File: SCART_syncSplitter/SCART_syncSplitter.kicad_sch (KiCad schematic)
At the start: 28 parts, among them J1 SCART-F, J2 VGA Out, J3 POWER IN, J4 HSync Selector, J5 Audio Out, U1 LMH1981, U2 L7805

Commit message: Assigned footprints
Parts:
- added C9: 10uF, Capacitor_THT:CP_Radial_D5.0mm_P2.50mm, symbol Device:C_Polarized_Small
- added JP2: VGA_PWR, Jumper:SolderJumper-2_P1.3mm_Open_RoundedPad1.0x1.5mm, symbol Jumper:SolderJumper_2_Open
- C8: value 10uF -> 4.7uF; footprint (none) -> Capacitor_THT:CP_Radial_D5.0mm_P2.50mm
- J2: footprint (none) -> Connector_Dsub:DSUB-15-HD_Female_Horizontal_P2.29x1.98mm_EdgePinOffset3.03mm_Housed_MountingHolesOffset4.94mm
- J3: footprint (none) -> Connector_BarrelJack:BarrelJack_Horizontal
- J4: footprint (none) -> Connector_PinHeader_2.54mm:PinHeader_2x02_P2.54mm_Vertical
- JP1: footprint (none) -> Connector_PinHeader_2.54mm:PinHeader_1x02_P2.54mm_Vertical
- TP1, TP2, TP3: footprint (none) -> TestPoint:TestPoint_Pad_1.0x1.0mm
- U2: footprint (none) -> Package_TO_SOT_SMD:TO-263-3_TabPin2
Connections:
- net GND: now also C9.2
- net VCC: now also C8.1, JP2.1 (A); no longer J2.9
- net at C7.1, J3.1 (In), U2.1 (IN): now also C9.1; no longer C8.1
- new net: J2.9, JP2.2 (B)
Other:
- moved on the sheet: C8
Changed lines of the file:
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@@
   (junction (at 97.79 39.37) (diameter 0) (color 0 0 0 0)
   )
+  (junction (at 135.89 24.13) (diameter 0) (color 0 0 0 0)
+  )
   (junction (at 19.05 137.16) (diameter 0) (color 0 0 0 0)
   )
@@
   )
   (junction (at 177.8 129.54) (diameter 0) (color 0 0 0 0)
+  )
+  (junction (at 128.27 39.37) (diameter 0) (color 0 0 0 0)
   )
   (junction (at 88.9 160.02) (diameter 0) (color 0 0 0 0)
@@
     (stroke (width 0) (type default))
   )
+  (wire (pts (xy 194.31 134.62) (xy 198.12 134.62))
+    (stroke (width 0) (type default))
+  )
   (wire (pts (xy 87.63 76.2) (xy 107.95 76.2))
     (stroke (width 0) (type default))
@@
     (stroke (width 0) (type default))
   )
+  (wire (pts (xy 128.27 39.37) (xy 135.89 39.37))
+    (stroke (width 0) (type default))
+  )
   (wire (pts (xy 198.12 129.54) (xy 177.8 129.54))
     (stroke (width 0) (type default))
@@
     (stroke (width 0) (type default))
   )
-  (wire (pts (xy 180.34 134.62) (xy 198.12 134.62))
+  (wire (pts (xy 135.89 39.37) (xy 135.89 34.29))
     (stroke (width 0) (type default))
   )
@@
     (stroke (width 0) (type default))
   )
+  (wire (pts (xy 180.34 134.62) (xy 186.69 134.62))
+    (stroke (width 0) (type default))
+  )
   (wire (pts (xy 120.65 130.81) (xy 120.65 134.62))
     (stroke (width 0) (type default))
@@
     (stroke (width 0) (type default))
   )
+  (wire (pts (xy 128.27 24.13) (xy 135.89 24.13))
+    (stroke (width 0) (type default))
+  )
   (wire (pts (xy 35.56 21.59) (xy 35.56 22.86))
     (stroke (width 0) (type default))
@@
     (stroke (width 0) (type default))
   )
+  (wire (pts (xy 135.89 24.13) (xy 135.89 29.21))
+    (stroke (width 0) (type default))
+  )
   (wire (pts (xy 184.15 127) (xy 198.12 127))
     (stroke (width 0) (type default))
@@
     (stroke (width 0) (type default))
   )
-  (wire (pts (xy 128.27 20.32) (xy 128.27 24.13))
+  (wire (pts (xy 135.89 20.32) (xy 135.89 24.13))
     (stroke (width 0) (type default))
   )
@@
       (effects (font (size 1.27 1.27)))
     )
-    (property "Footprint" "" (at 181.61 121.92 0)
+    (property "Footprint" "Connector_Dsub:DSUB-15-HD_Female_Horizontal_P2.29x1.98mm_EdgePinOffset3.03mm_Housed_MountingHolesOffset4.94mm" (at 181.61 121.92 0)
       (effects (font (size 1.27 1.27)) hide)
     )
@@
       (effects (font (size 1.27 1.27)) (justify left))
     )
-    (property "Footprint" "" (at 77.47 54.61 0)
+    (property "Footprint" "TestPoint:TestPoint_Pad_1.0x1.0mm" (at 77.47 54.61 0)
       (effects (font (size 1.27 1.27)) hide)
     )
@@
       (effects (font (size 1.27 1.27)))
     )
-    (property "Footprint" "" (at 240.03 135.89 0)
+    (property "Footprint" "Connector_PinHeader_2.54mm:PinHeader_2x02_P2.54mm_Vertical" (at 240.03 135.89 0)
       (effects (font (size 1.27 1.27)) hide)
     )
@@
     )
   )
-  (symbol (lib_id "power:VCC") (at 128.27 20.32 0) (unit 1)
+  (symbol (lib_id "power:VCC") (at 135.89 20.32 0) (unit 1)
     (in_bom yes) (on_board yes) (dnp no) (fields_autoplaced)
-    (property "Reference" "#PWR012" (at 128.27 24.13 0)
-      (effects (font (size 1.27 1.27)) hide)
-    )
-    (property "Value" "VCC" (at 128.27 15.24 0)
-      (effects (font (size 1.27 1.27)))
-    )
-    (property "Footprint" "" (at 128.27 20.32 0)
-      (effects (font (size 1.27 1.27)) hide)
-    )
-    (property "Datasheet" "" (at 128.27 20.32 0)
+    (property "Reference" "#PWR012" (at 135.89 24.13 0)
+      (effects (font (size 1.27 1.27)) hide)
+    )
+    (property "Value" "VCC" (at 135.89 15.24 0)
+      (effects (font (size 1.27 1.27)))
+    )
+    (property "Footprint" "" (at 135.89 20.32 0)
+      (effects (font (size 1.27 1.27)) hide)
+    )
+    (property "Datasheet" "" (at 135.89 20.32 0)
       (effects (font (size 1.27 1.27)) hide)
     )
@@
       (effects (font (size 1.27 1.27)) (justify left))
     )
-    (property "Footprint" "" (at 88.9 33.02 0)
+    (property "Footprint" "Connector_BarrelJack:BarrelJack_Horizontal" (at 88.9 33.02 0)
       (effects (font (size 1.27 1.27)) hide)
     )
@@
       (effects (font (size 1.27 1.27)))
     )
-    (property "Footprint" "" (at 114.935 27.94 0)
+    (property "Footprint" "Package_TO_SOT_SMD:TO-263-3_TabPin2" (at 114.935 27.94 0)
       (effects (font (size 1.27 1.27) italic) (justify left) hide)
     )
@@
     )
   )
+  (symbol (lib_id "Device:C_Polarized_Small") (at 97.79 31.75 0) (unit 1)
+    (in_bom yes) (on_board yes) (dnp no)
+    (property "Reference" "C9" (at 95.25 33.02 90)
+      (effects (font (size 1.27 1.27)) (justify left))
+    )
+    (property "Value" "10uF" (at 100.33 34.29 90)
+      (effects (font (size 1.27 1.27)) (justify left))
+    )
+    (property "Footprint" "Capacitor_THT:CP_Radial_D5.0mm_P2.50mm" (at 97.79 31.75 0)
+      (effects (font (size 1.27 1.27)) hide)
+    )
+    (property "Datasheet" "~" (at 97.79 31.75 0)
+      (effects (font (size 1.27 1.27)) hide)
+    )
+    (pin "1")
+    (pin "2")
+    (instances
+      (project "SCART_syncSplitter"
+        (path "/99f02354-cbc7-4051-afde-370f4d1f5517"
+          (reference "C9") (unit 1)
+        )
+      )
+    )
+  )
   (symbol (lib_id "power:GND") (at 120.65 134.62 0) (unit 1)
     (in_bom yes) (on_board yes) (dnp no) (fields_autoplaced)
@@
       (effects (font (size 1.27 1.27)) (justify left))
     )
-    (property "Footprint" "" (at 113.03 66.04 0)
+    (property "Footprint" "TestPoint:TestPoint_Pad_1.0x1.0mm" (at 113.03 66.04 0)
       (effects (font (size 1.27 1.27)) hide)
     )
@@
         (path "/99f02354-cbc7-4051-afde-370f4d1f5517"
           (reference "TP3") (unit 1)
+        )
+      )
+    )
+  )
+  (symbol (lib_id "Jumper:SolderJumper_2_Open") (at 190.5 134.62 0) (unit 1)
+    (in_bom yes) (on_board yes) (dnp no)
+    (property "Reference" "JP2" (at 186.69 133.35 0)
+      (effects (font (size 1.27 1.27)))
+    )
+    (property "Value" "VGA_PWR" (at 195.58 133.35 0)
+      (effects (font (size 1.27 1.27)))
+    )
+    (property "Footprint" "Jumper:SolderJumper-2_P1.3mm_Open_RoundedPad1.0x1.5mm" (at 190.5 134.62 0)
+      (effects (font (size 1.27 1.27)) hide)
+    )
+    (property "Datasheet" "~" (at 190.5 134.62 0)
+      (effects (font (size 1.27 1.27)) hide)
+    )
+    (pin "1")
+    (pin "2")
+    (instances
+      (project "SCART_syncSplitter"
+        (path "/99f02354-cbc7-4051-afde-370f4d1f5517"
+          (reference "JP2") (unit 1)
         )
       )
@@
       (effects (font (size 1.27 1.27)) (justify left))
     )
-    (property "Footprint" "" (at 80.01 54.61 0)
+    (property "Footprint" "TestPoint:TestPoint_Pad_1.0x1.0mm" (at 80.01 54.61 0)
       (effects (font (size 1.27 1.27)) hide)
     )
@@
     )
   )
-  (symbol (lib_id "Device:C_Polarized_Small") (at 97.79 31.75 0) (unit 1)
-    (in_bom yes) (on_board yes) (dnp no)
-    (property "Reference" "C8" (at 95.25 33.02 90)
-      (effects (font (size 1.27 1.27)) (justify left))
-    )
-    (property "Value" "10uF" (at 100.33 34.29 90)
-      (effects (font (size 1.27 1.27)) (justify left))
-    )
-    (property "Footprint" "" (at 97.79 31.75 0)
-      (effects (font (size 1.27 1.27)) hide)
-    )
-    (property "Datasheet" "~" (at 97.79 31.75 0)
+  (symbol (lib_id "Device:C_Polarized_Small") (at 135.89 31.75 0) (unit 1)
+    (in_bom yes) (on_board yes) (dnp no)
+    (property "Reference" "C8" (at 133.35 33.02 90)
+      (effects (font (size 1.27 1.27)) (justify left))
+    )
+    (property "Value" "4.7uF" (at 138.43 34.29 90)
+      (effects (font (size 1.27 1.27)) (justify left))
+    )
+    (property "Footprint" "Capacitor_THT:CP_Radial_D5.0mm_P2.50mm" (at 135.89 31.75 0)
+      (effects (font (size 1.27 1.27)) hide)
+    )
+    (property "Datasheet" "~" (at 135.89 31.75 0)
       (effects (font (size 1.27 1.27)) hide)
     )
@@
       (effects (font (size 1.27 1.27)))
     )
-    (property "Footprint" "" (at 231.14 132.08 0)
-      (effects (font (size 1.27 1.27)) hide)
-    )
+    (property "Footprint" "Connector_PinHeader_2.54mm:PinHeader_1x02_P2.54mm_Vertical" (at 231.14 132.08 0)
+      (effects (font (size 1.27 1.27)) hide)
+    )

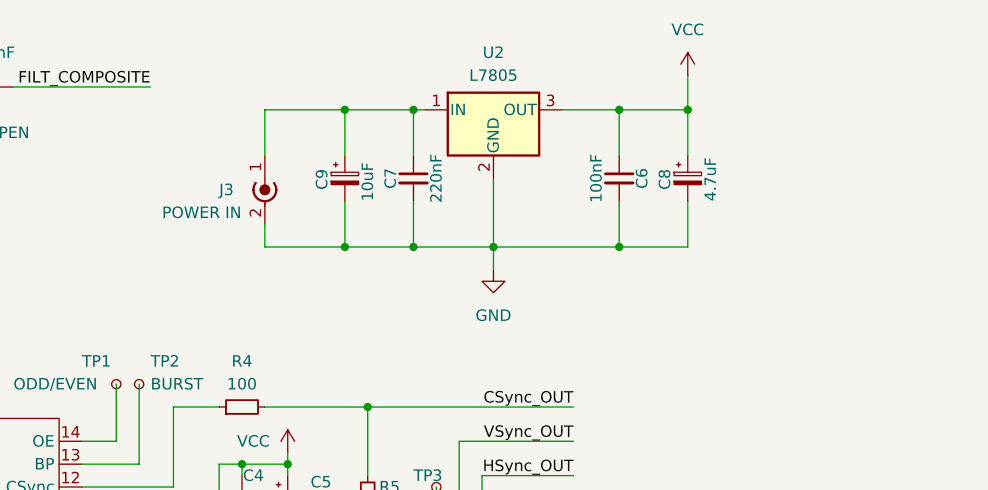
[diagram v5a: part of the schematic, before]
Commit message: Start preparing the PCB
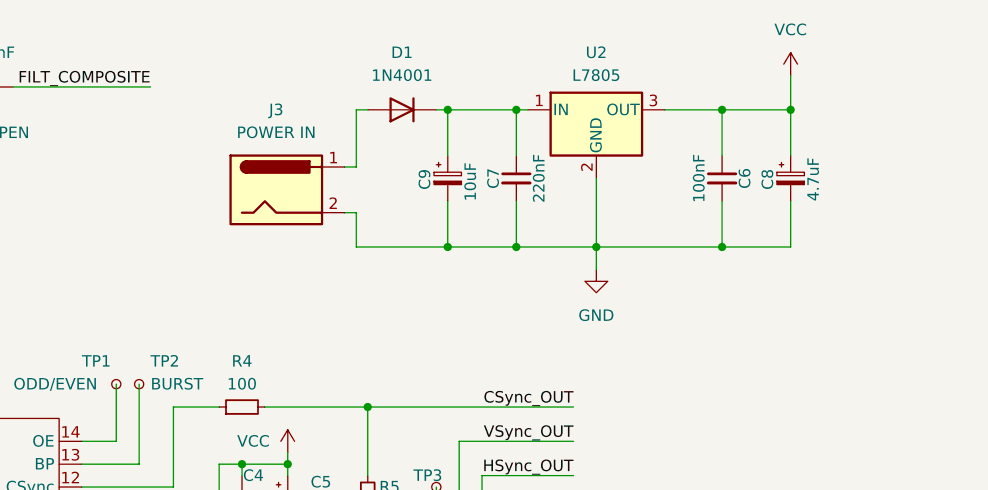
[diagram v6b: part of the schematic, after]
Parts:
- removed J3: POWER IN, Connector_BarrelJack:BarrelJack_Horizontal, symbol Connector:Conn_Coaxial_Power
- added D1: 1N4001, Diode_THT:D_DO-41_SOD81_P10.16mm_Horizontal, symbol Diode:1N4001
- added J3: POWER IN, Connector_BarrelJack:BarrelJack_Horizontal, symbol Connector:Barrel_Jack
- C5: footprint (none) -> Capacitor_THT:CP_Radial_D5.0mm_P2.50mm
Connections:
- net GND: now also J3.2
- net at C7.1, C9.1, U2.1 (IN): now also D1.1 (K)
- new net: D1.2 (A), J3.1
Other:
- moved on the sheet: C6, C7, C8, C9, U2

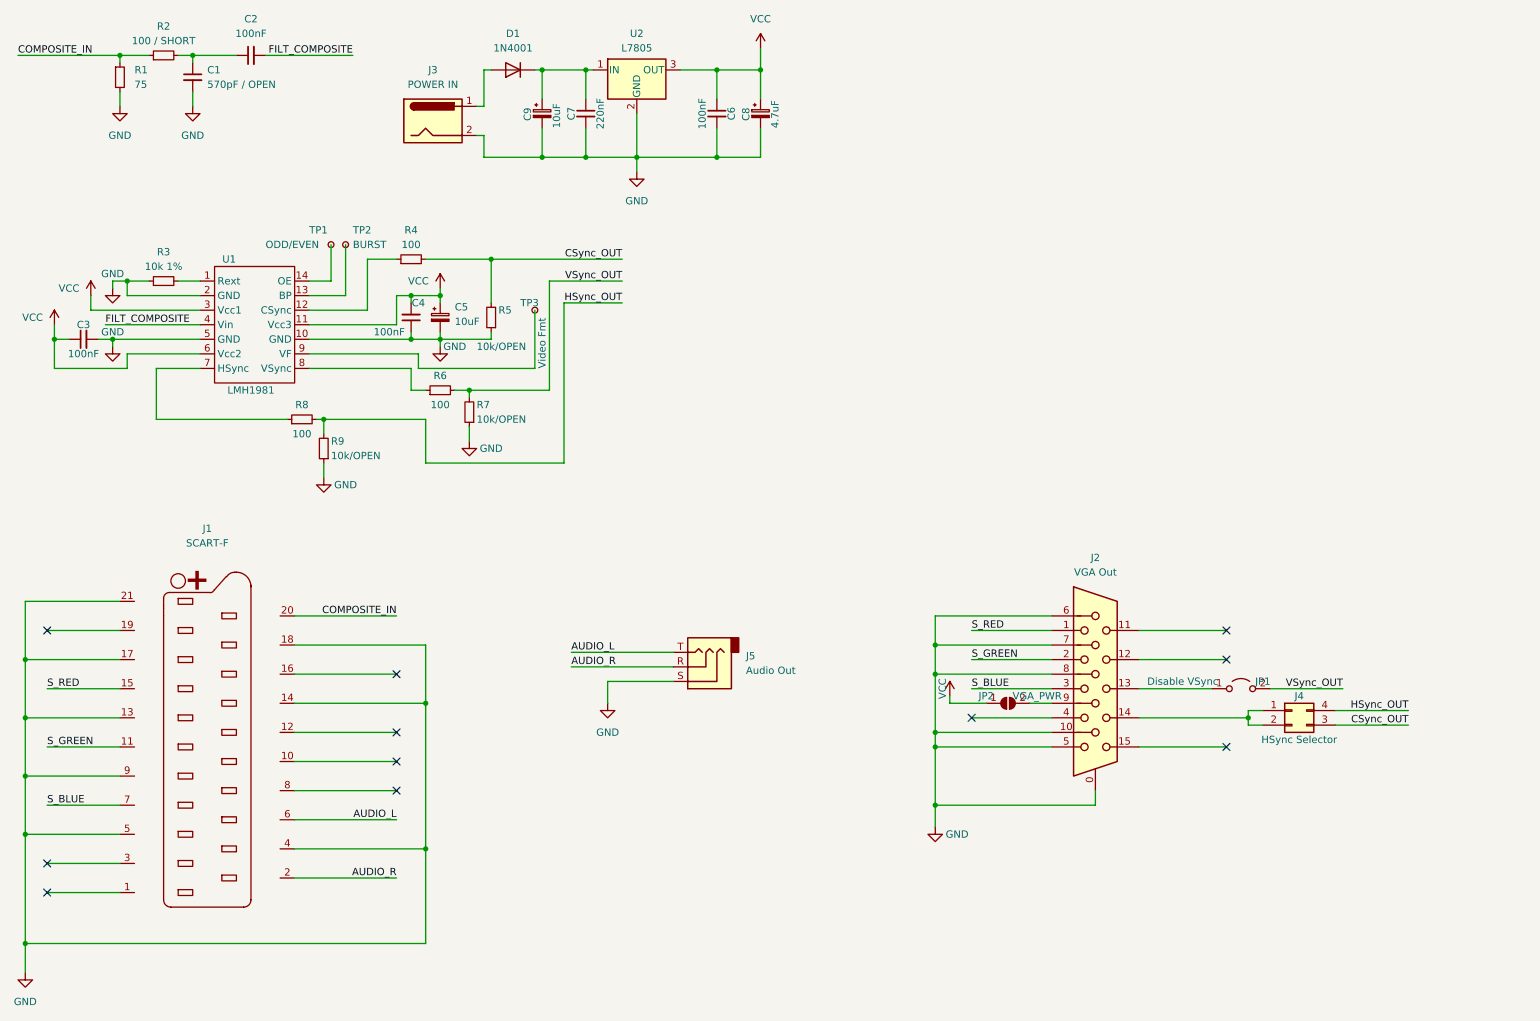
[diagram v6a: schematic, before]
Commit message: Add Power led
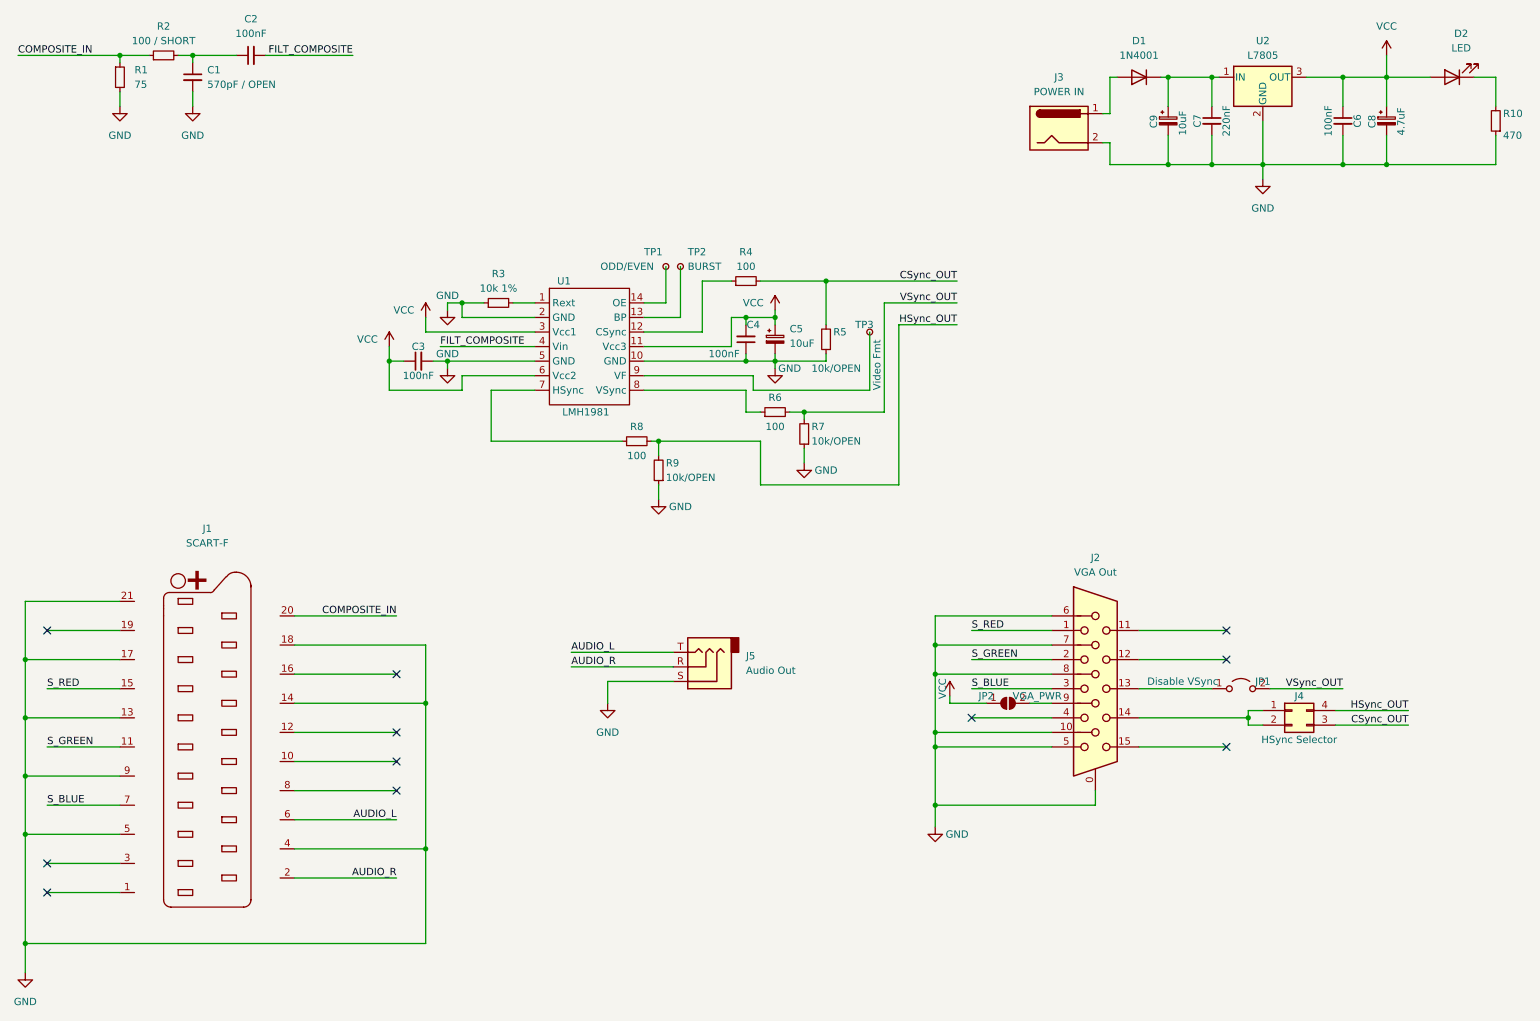
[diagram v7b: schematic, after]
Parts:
- added D2: LED, LED_SMD:LED_1206_3216Metric_Pad1.42x1.75mm_HandSolder, symbol Device:LED
- added R10: 470, Resistor_SMD:R_1206_3216Metric_Pad1.30x1.75mm_HandSolder, symbol Device:R_Small
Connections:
- net GND: now also R10.1
- net VCC: now also D2.2 (A)
- new net: D2.1 (K), R10.2
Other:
- moved on the sheet: C3, C4, C5, C6, C7, C8, C9, D1, J3, R3, R4, R5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

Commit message: Update PCB and schematic
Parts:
- C1: value 570pF / OPEN -> 570pF
- JP1: value Disable VSync -> Enable VSync
- R2: value 100 / SHORT -> 100
- R5, R7, R9: value 10k/OPEN -> OPEN
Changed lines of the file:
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@@
       (effects (font (size 1.27 1.27)) (justify right))
     )
-    (property "Value" "10k/OPEN" (at 130.81 95.25 0)
+    (property "Value" "OPEN" (at 130.81 95.25 0)
       (effects (font (size 1.27 1.27)) (justify right))
     )
@@
       (effects (font (size 1.27 1.27)) (justify right))
     )
-    (property "Value" "10k/OPEN" (at 156.21 76.2 0)
+    (property "Value" "OPEN" (at 156.21 76.2 0)
       (effects (font (size 1.27 1.27)) (justify right))
     )
@@
       (effects (font (size 1.27 1.27)))
     )
-    (property "Value" "100 / SHORT" (at 43.18 19.05 90)
+    (property "Value" "100" (at 43.18 19.05 90)
       (effects (font (size 1.27 1.27)))
     )
@@
       (effects (font (size 1.27 1.27)) (justify left))
     )
-    (property "Value" "570pF / OPEN" (at 50.8 26.6763 0)
+    (property "Value" "570pF" (at 50.8 26.6763 0)
       (effects (font (size 1.27 1.27)) (justify left))
     )
@@
       (effects (font (size 1.27 1.27)))
     )
-    (property "Value" "Disable VSync" (at 220.98 130.81 0)
+    (property "Value" "Enable VSync" (at 220.98 130.81 0)
       (effects (font (size 1.27 1.27)))
     )
@@
       (effects (font (size 1.27 1.27)) (justify right))
     )
-    (property "Value" "10k/OPEN" (at 156.21 88.9 0)
+    (property "Value" "OPEN" (at 156.21 88.9 0)
       (effects (font (size 1.27 1.27)) (justify right))
     )
